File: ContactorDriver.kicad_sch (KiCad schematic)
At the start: 49 parts, among them J1 PowerConn, J2 DashboardConn, J3 ContactorConn, J4 PrechargeResistorConn, J5 PrechargeResistor, J6 PrechargeResistor, Q1 CSD18511KTT, Q2 PMOS, Q3 PMOS, Q4 CSD18511KTT, U1 RI3-1212S, U2 OPAx192-Q1, U3 OPAx192-Q1

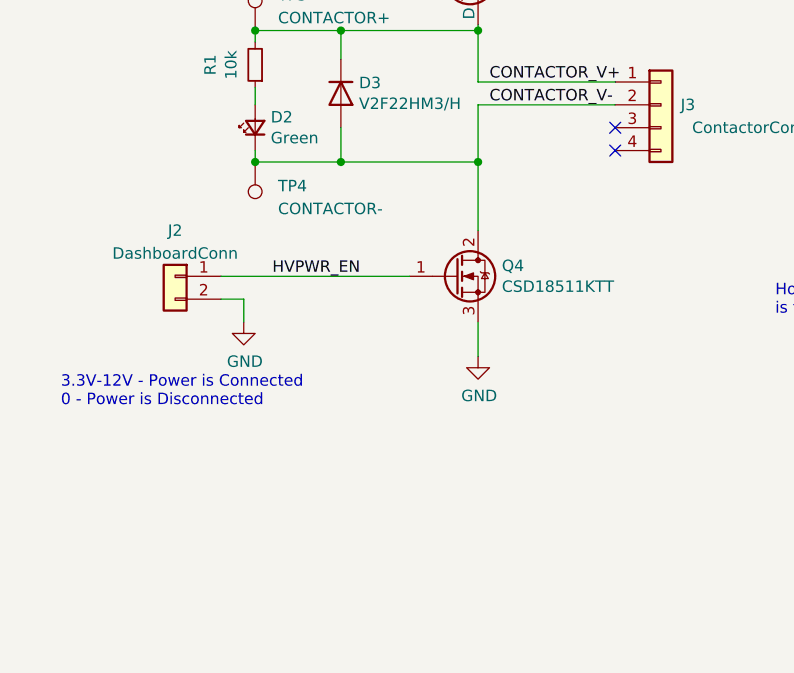
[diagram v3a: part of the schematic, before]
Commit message: Changed input control logic
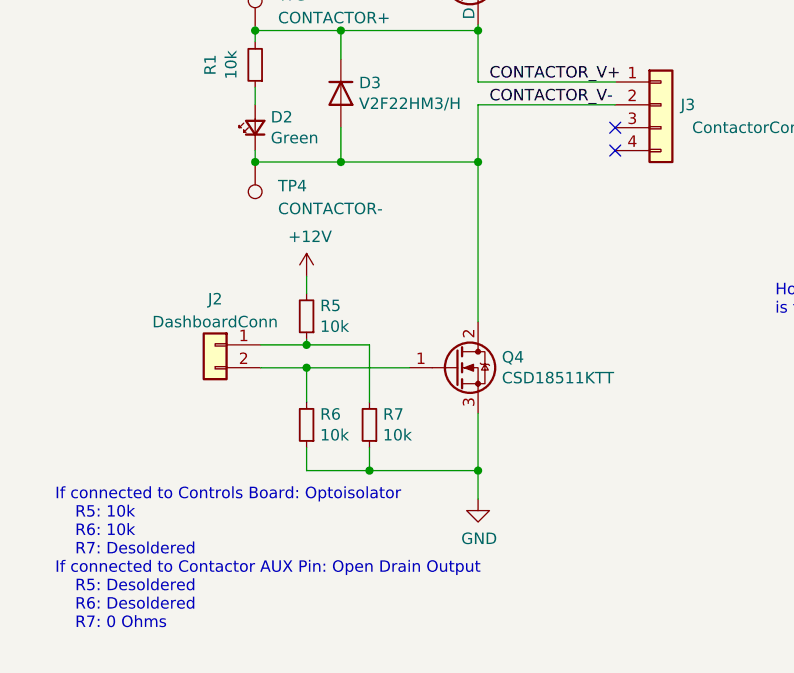
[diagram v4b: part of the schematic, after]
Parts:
- added R5, R6, R7: 10k, Resistor_SMD:R_0805_2012Metric_Pad1.15x1.40mm_HandSolder, symbol Device:R_Small
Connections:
- net +12V: now also R5.2
- net GND: now also R6.1, R7.1; no longer J2.2 (Pin_2)
- net HVPWR_EN: no longer names the net of J2.1 (Pin_1)
- net HVPWR_EN: now also R5.1, R7.2; no longer Q4.1 (G)
- new net: J2.2 (Pin_2), Q4.1 (G), R6.2
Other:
- note added: "If connected to Controls Board: Optoisolator R5: 10k R6: 10k R7: Desoldered If connected to Contactor AUX Pin: Open Drain Output R5: Desoldered R6: Desoldered R7: 0 Ohms"
- note removed: "3.3V-12V - Power is Connected 0 - Power is Disconnected"
- moved on the sheet: J2, Q4

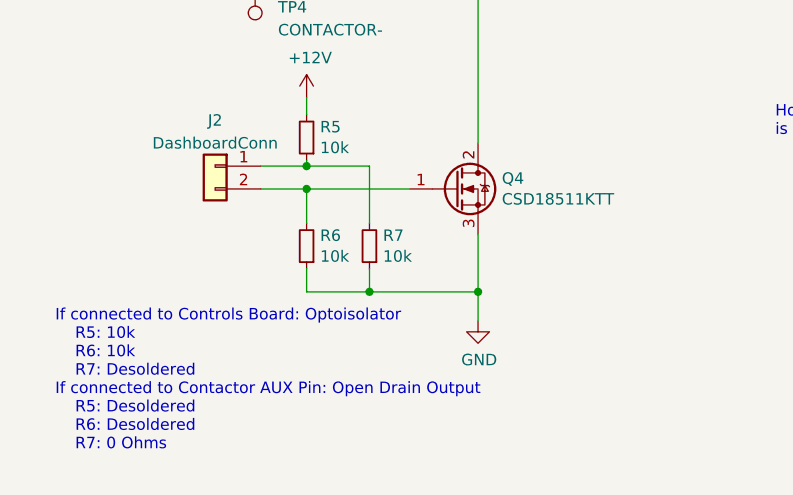
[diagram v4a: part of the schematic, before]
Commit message: Changed input logic to normally open
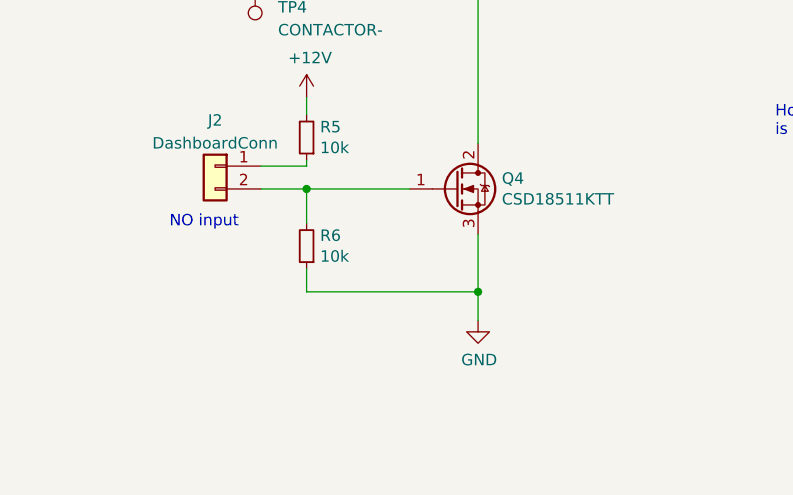
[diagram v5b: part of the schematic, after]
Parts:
- removed R7: 10k, Resistor_SMD:R_0805_2012Metric_Pad1.15x1.40mm_HandSolder, symbol Device:R_Small
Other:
- note added: "NO input"
- note removed: "If connected to Controls Board: Optoisolator R5: 10k R6: 10k R7: Desoldered If connected to Contactor AUX Pin: Open Drain Output R5: Desoldered R6: Desoldered R7: 0 Ohms"
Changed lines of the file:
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@@
   (junction (at 131.445 153.035) (diameter 0) (color 0 0 0 0)
   )
-  (junction (at 44.45 140.97) (diameter 0) (color 0 0 0 0)
-  )
   (junction (at 137.16 83.82) (diameter 0) (color 0 0 0 0)
   )
@@
   )
   (junction (at 113.665 44.45) (diameter 0) (color 0 0 0 0)
-  )
-  (junction (at 51.435 154.94) (diameter 0) (color 0 0 0 0)
   )
   (junction (at 48.895 38.1) (diameter 0) (color 0 0 0 0)
@@
     (stroke (width 0) (type default))
   )
-  (wire (pts (xy 51.435 154.94) (xy 63.5 154.94))
-    (stroke (width 0) (type default))
-  )
   (wire (pts (xy 63.5 111.76) (xy 63.5 106.045))
     (stroke (width 0) (type default))
@@
     (stroke (width 0) (type default))
   )
-  (wire (pts (xy 51.435 140.97) (xy 51.435 147.32))
-    (stroke (width 0) (type default))
-  )
   (wire (pts (xy 140.97 96.52) (xy 140.97 97.155))
     (stroke (width 0) (type default))
@@
     (stroke (width 0) (type default))
   )
-  (wire (pts (xy 51.435 154.94) (xy 51.435 152.4))
-    (stroke (width 0) (type default))
-  )
   (wire (pts (xy 205.74 83.82) (xy 213.995 83.82))
     (stroke (width 0) (type default))
@@
     (stroke (width 0) (type default))
   )
-  (wire (pts (xy 44.45 154.94) (xy 51.435 154.94))
+  (wire (pts (xy 44.45 154.94) (xy 63.5 154.94))
     (stroke (width 0) (type default))
   )
@@
   )
   (wire (pts (xy 27.94 45.72) (xy 43.815 45.72))
-    (stroke (width 0) (type default))
-  )
-  (wire (pts (xy 44.45 140.97) (xy 51.435 140.97))
     (stroke (width 0) (type default))
   )
@@
     (effects (font (size 1.2446 1.2446)) (justify left bottom))
   )
-  (text "If connected to Controls Board: Optoisolator\n	R5: 10k\n	R6: 10k\n	R7: Desoldered\nIf connected to Contactor AUX Pin: Open Drain Output\n	R5: Desoldered\n	R6: Desoldered\n	R7: 0 Ohms"
-    (at 16.51 172.72 0)
+  (text "NO input" (at 29.21 147.955 0)
     (effects (font (size 1.27 1.27)) (justify left bottom))
   )
@@
         )
       )
-    )
-  )
-  (symbol (lib_id "Device:R_Small") (at 51.435 149.86 180) (unit 1)
-    (in_bom yes) (on_board yes) (dnp no)
-    (property "Reference" "R7" (at 52.9336 148.6916 0)
-      (effects (font (size 1.27 1.27)) (justify right))
-    )
-    (property "Value" "10k" (at 52.9336 151.003 0)
-      (effects (font (size 1.27 1.27)) (justify right))
-    )
-    (property "Footprint" "Resistor_SMD:R_0805_2012Metric_Pad1.15x1.40mm_HandSolder" (at 51.435 149.86 0)
-      (effects (font (size 1.27 1.27)) hide)
-    )
-    (property "Datasheet" "https://www.mouser.com/datasheet/2/210/Kamaya_RMC_automotive_series_8_2022__1_-3032429.pdf" (at 51.435 149.86 0)
-      (effects (font (size 1.27 1.27)) hide)
-    )
-    (pin "1")
-    (pin "2")
-    (instances
-      (project "ContactorDriver"
-        (path "/aaa5c8ef-bb12-4c4a-bd2b-ddbca3d09ae8"
-          (reference "R7") (unit 1)
-        )
-      )

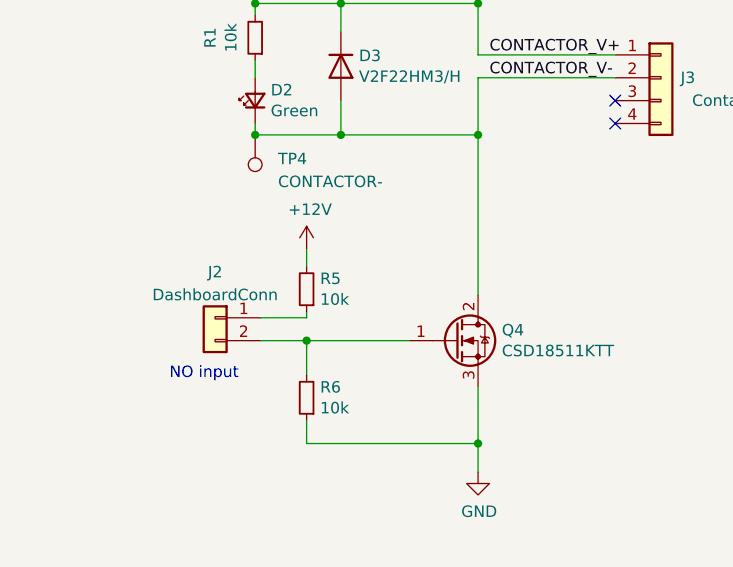
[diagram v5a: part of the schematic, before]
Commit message: Removed PU resistor
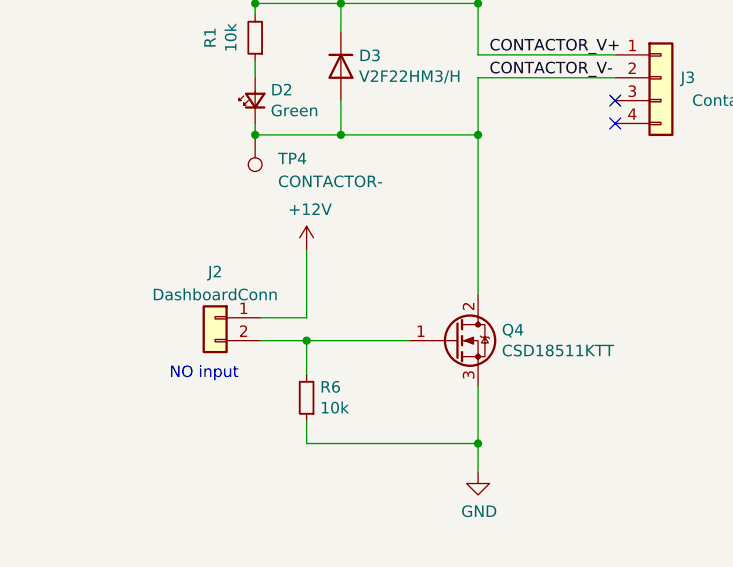
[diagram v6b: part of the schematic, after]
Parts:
- removed R5: 10k, Resistor_SMD:R_0805_2012Metric_Pad1.15x1.40mm_HandSolder, symbol Device:R_Small
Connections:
- net +12V: now also J2.1 (Pin_1)
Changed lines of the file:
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@@
-    (stroke (width 0) (type default))
-  )
-  (wire (pts (xy 44.45 133.35) (xy 44.45 135.255))
     (stroke (width 0) (type default))
   )
@@
     (stroke (width 0) (type default))
   )
-  (wire (pts (xy 44.45 140.97) (xy 44.45 140.335))
+  (wire (pts (xy 44.45 133.35) (xy 44.45 140.97))
     (stroke (width 0) (type default))
   )
@@
         )
       )
-    )
-  )
-  (symbol (lib_id "Device:R_Small") (at 44.45 137.795 180) (unit 1)
-    (in_bom yes) (on_board yes) (dnp no)
-    (property "Reference" "R5" (at 45.9486 136.6266 0)
-      (effects (font (size 1.27 1.27)) (justify right))
-    )
-    (property "Value" "10k" (at 45.9486 138.938 0)
-      (effects (font (size 1.27 1.27)) (justify right))
-    )
-    (property "Footprint" "Resistor_SMD:R_0805_2012Metric_Pad1.15x1.40mm_HandSolder" (at 44.45 137.795 0)
-      (effects (font (size 1.27 1.27)) hide)
-    )
-    (property "Datasheet" "https://www.mouser.com/datasheet/2/210/Kamaya_RMC_automotive_series_8_2022__1_-3032429.pdf" (at 44.45 137.795 0)
-      (effects (font (size 1.27 1.27)) hide)
-    )
-    (pin "1")
-    (pin "2")
-    (instances
-      (project "ContactorDriver"
-        (path "/aaa5c8ef-bb12-4c4a-bd2b-ddbca3d09ae8"
-          (reference "R5") (unit 1)
-        )
-      )

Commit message: Moved comments
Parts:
- R6: value 10k -> 100k
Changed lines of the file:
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@@
     (effects (font (size 1.27 1.27)) (justify left bottom))
   )
-  (text "Min Vin = -.5V" (at 263.525 82.55 0)
+  (text "Min Vin = -.5V" (at 222.25 93.345 0)
     (effects (font (size 1.27 1.27)) (justify left bottom))
   )
@@
     (effects (font (size 2.54 2.54) (thickness 0.508) bold) (justify left bottom))
   )
-  (text "Min Vin = -.5V" (at 186.69 82.55 0)
+  (text "Min Vin = -.5V" (at 144.78 93.98 0)
     (effects (font (size 1.27 1.27)) (justify left bottom))
   )
@@
       (effects (font (size 1.27 1.27)) (justify right))
     )
-    (property "Value" "10k" (at 45.9486 151.003 0)
+    (property "Value" "100k" (at 45.9486 151.003 0)
       (effects (font (size 1.27 1.27)) (justify right))
     )

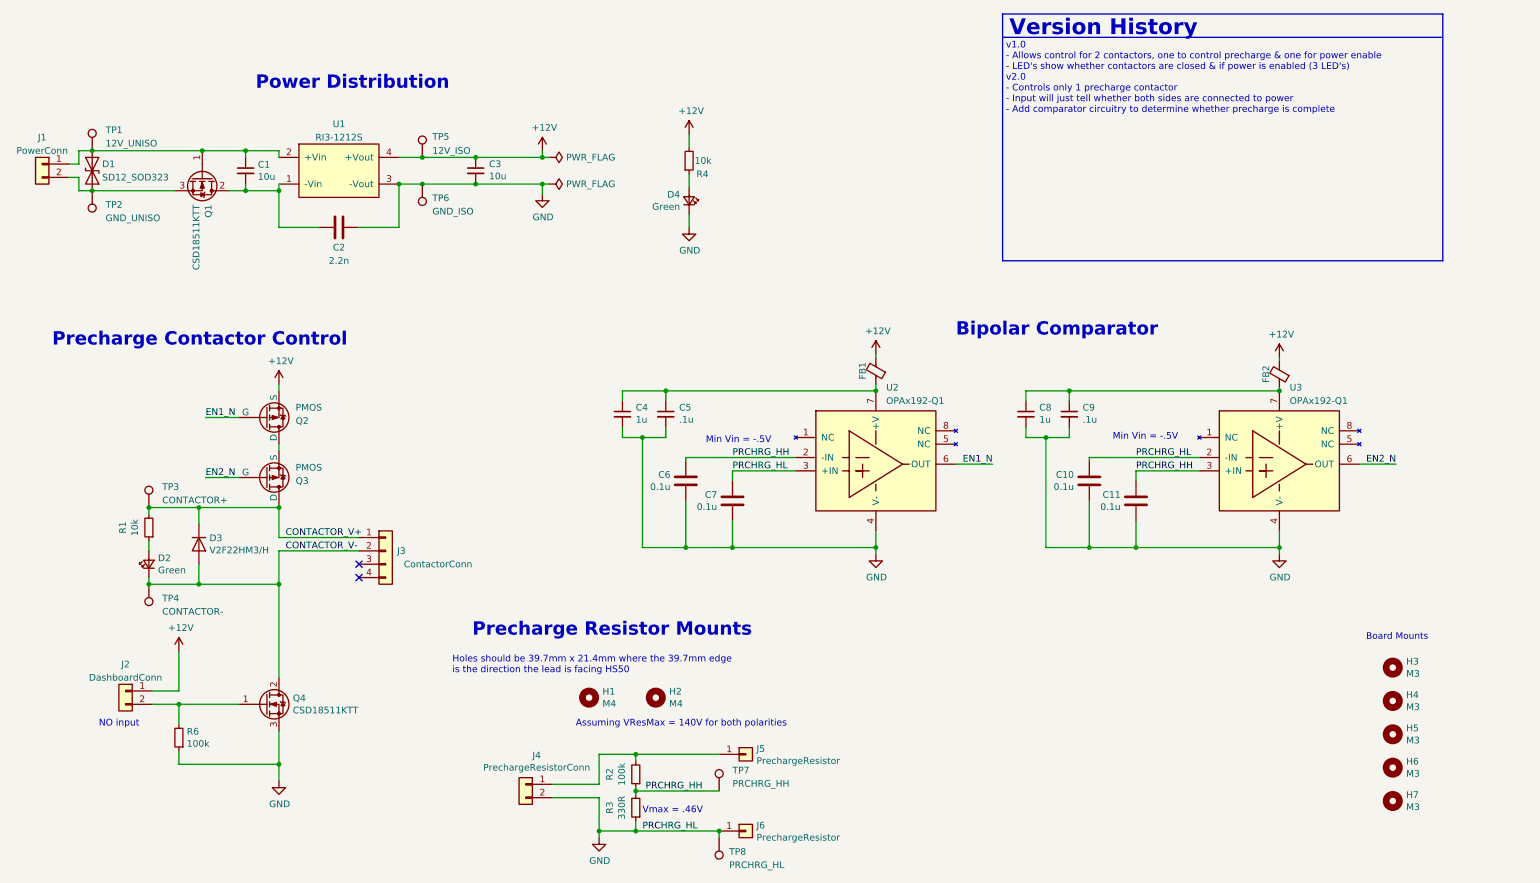
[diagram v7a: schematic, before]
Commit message: Used INA instead of 2 comparators
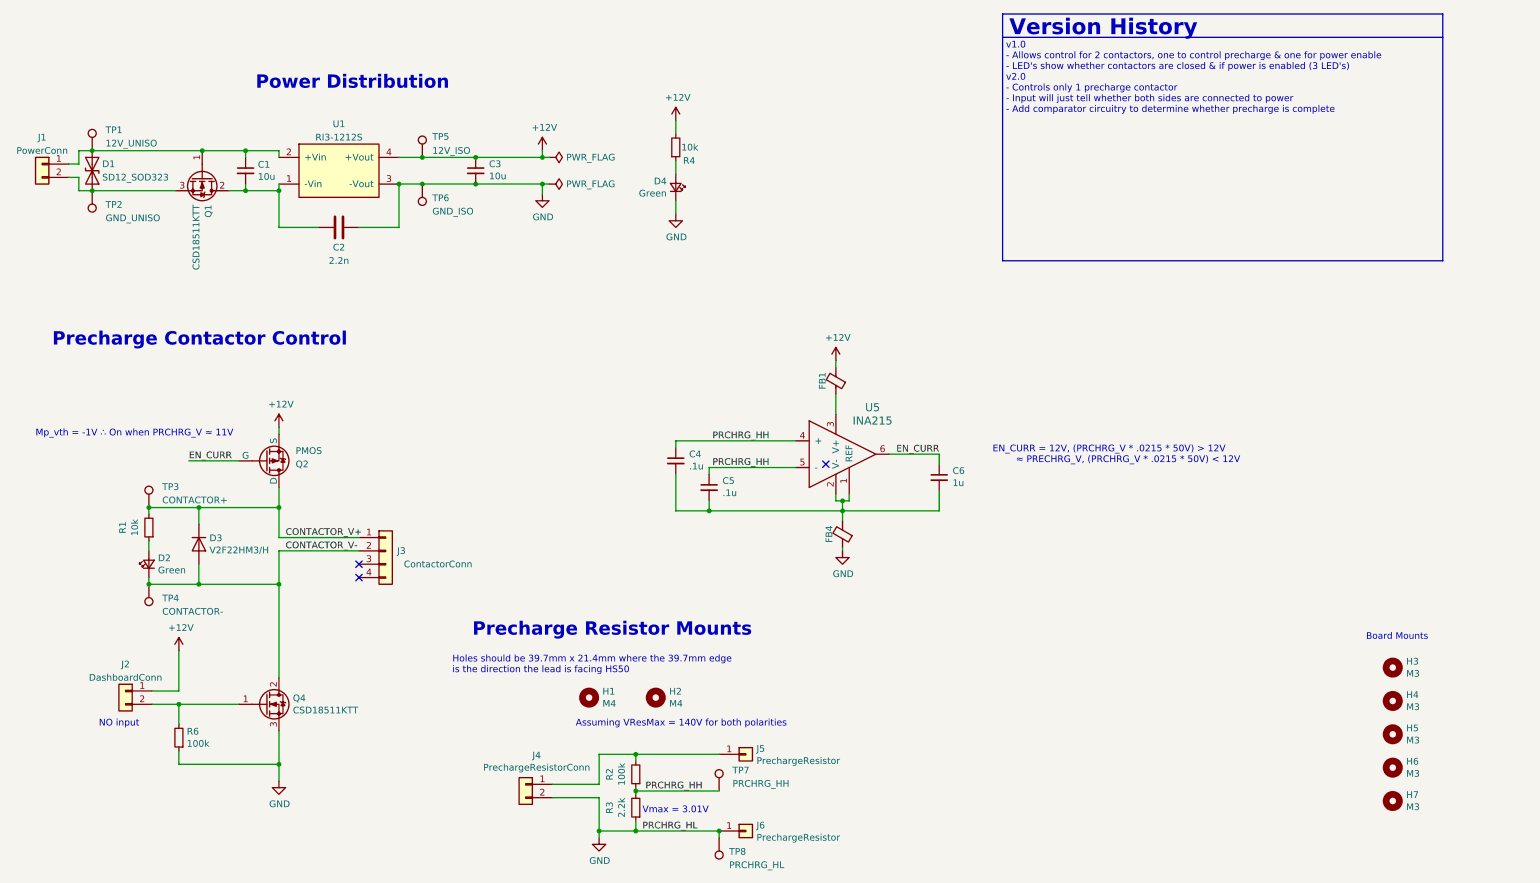
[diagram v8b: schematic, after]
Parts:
- removed C10, C11, C6, C7: 0.1u, Capacitor_SMD:C_0805_2012Metric, symbol Device:C
- removed C8: 1u, Capacitor_SMD:C_0805_2012Metric, symbol Device:C_Small
- removed C9: .1u, Capacitor_SMD:C_0805_2012Metric, symbol Device:C_Small
- removed FB2: FerriteBead_Small, Inductor_SMD:L_0805_2012Metric, symbol Device:FerriteBead_Small
- removed Q3: PMOS, Package_TO_SOT_THT:TO-220-3_Vertical, symbol Simulation_SPICE:PMOS
- removed U2, U3: OPAx192-Q1, Package_SO:VSSOP-8_3.0x3.0mm_P0.65mm, symbol utsvt-chips:OPAx192-Q1
- added C6: 1u, Capacitor_SMD:C_0805_2012Metric, symbol Device:C_Small
- added FB4: FerriteBead_Small, Inductor_SMD:L_0805_2012Metric, symbol Device:FerriteBead_Small
- added U5: INA215, symbol utsvt-chips:INA21x
- C4: value 1u -> .1u
- R3: value 330R -> 2.2k
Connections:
- net CONTACTOR_V+: now also Q2.1 (D)
- net GND: now also FB4.1; no longer C4.2, C5.2
- net PRCHRG_HH: now also C4.1, C5.1, U5.4 (+), U5.5 (-)
- net EN1_N renamed EN_CURR
- net EN_CURR: now also C6.1, U5.6
- new net: C4.2, C5.2, C6.2, FB4.2, U5.1 (REF), U5.2 (V-)
- new net: FB1.1, U5.3 (V+)
- no-connect marks 2 -> 3
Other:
- note added: "EN_CURR = 12V, (PRCHRG_V * .0215 * 50V) > 12V ≈ PRECHRG_V, (PRCHRG_V * .0215 * 50V) < 12V"
- note added: "Mp_vth = -1V ∴ On when PRCHRG_V ≈ 11V"
- note added: "Vmax = 3.01V"
- note removed: "Bipolar Comparator"
- note removed: "Min Vin = -.5V"
- note removed: "Vmax = .46V"
- moved on the sheet: D4, Q2, R4
